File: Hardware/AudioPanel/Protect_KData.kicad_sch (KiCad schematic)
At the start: 34 parts

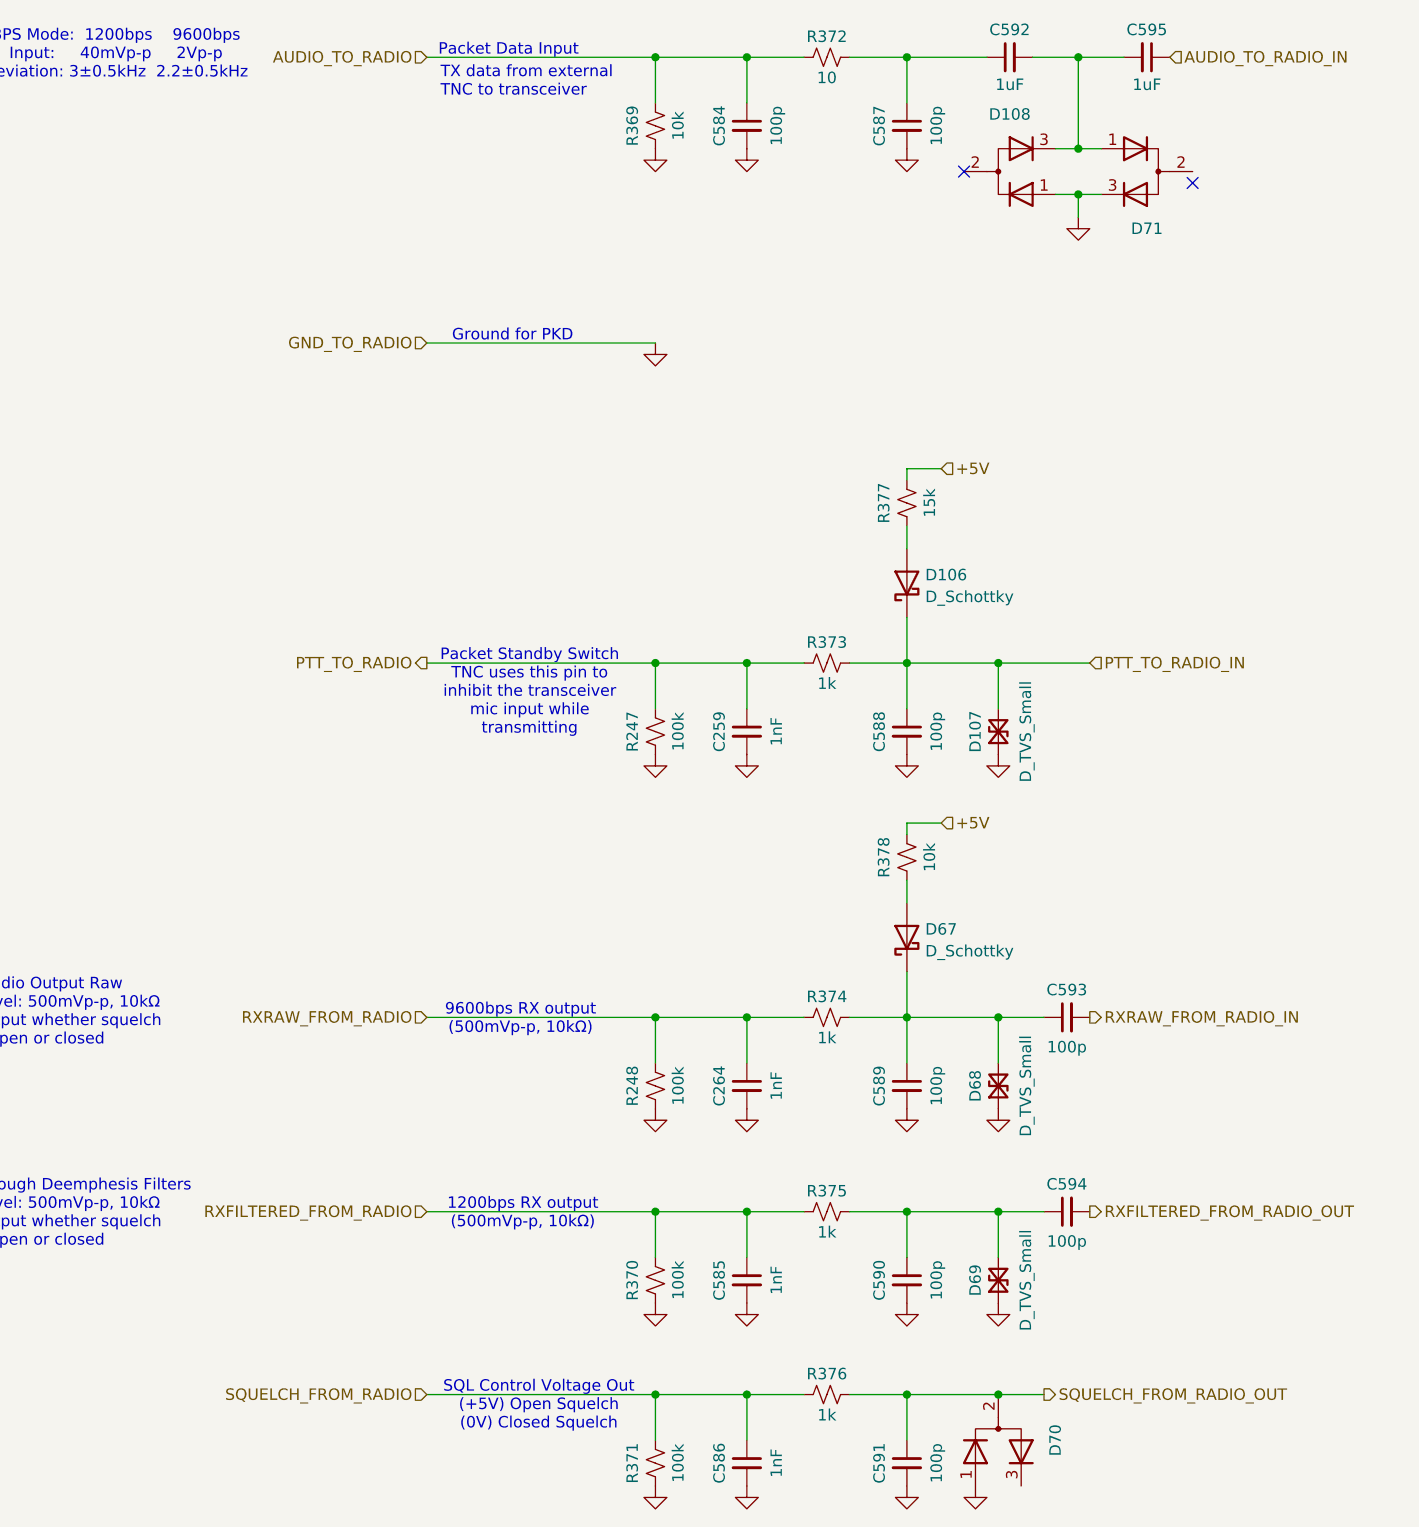
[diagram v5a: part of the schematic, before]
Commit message: Realized that I need to rethink how I'm going to mix the radio audio with the stereo audio
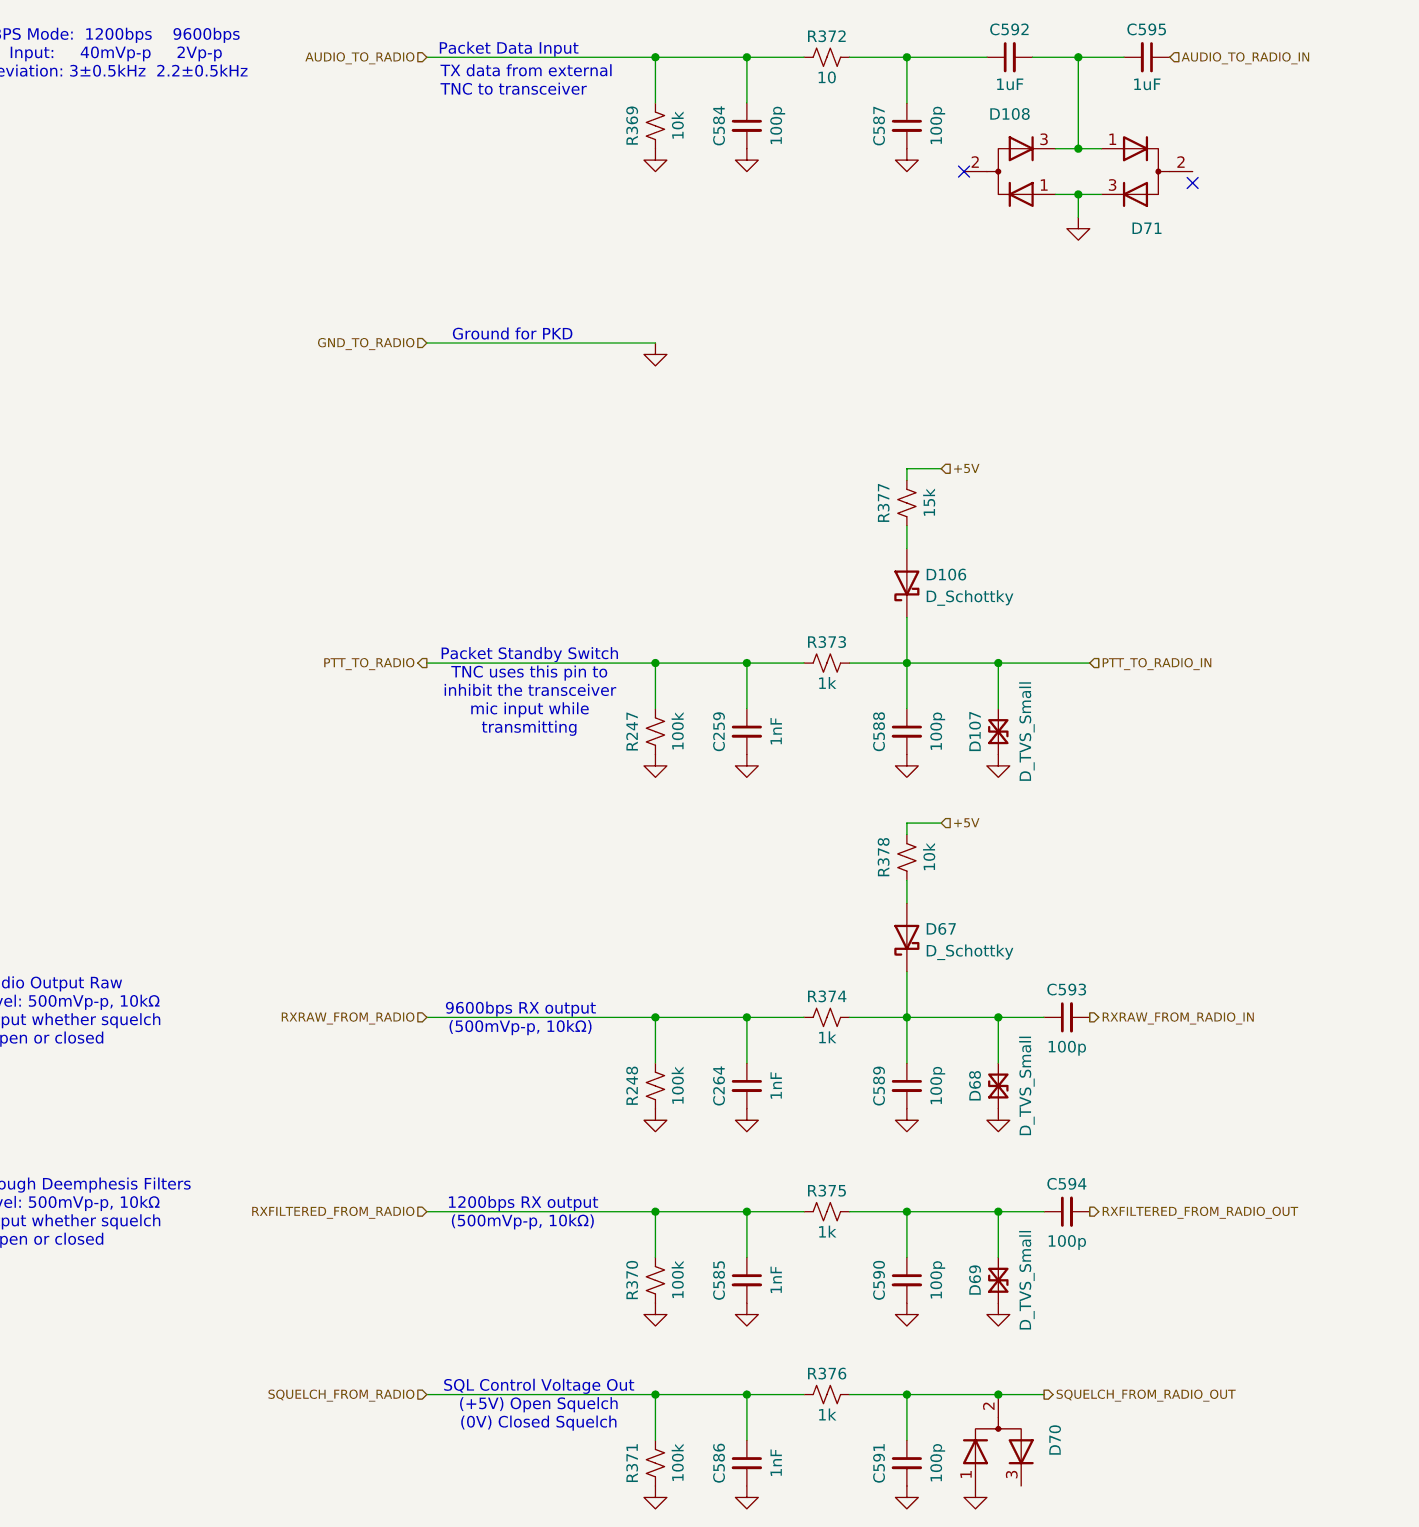
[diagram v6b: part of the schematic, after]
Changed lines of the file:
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@@
 		(effects
 			(font
-				(size 1.27 1.27)
+				(size 1 1)
 			)
 			(justify right)
@@
 		(effects
 			(font
-				(size 1.27 1.27)
+				(size 1 1)
 			)
 			(justify left)
@@
 		(effects
 			(font
-				(size 1.27 1.27)
+				(size 1 1)
 			)
 			(justify right)
@@
 		(effects
 			(font
-				(size 1.27 1.27)
+				(size 1 1)
 			)
 			(justify left)
@@
 		(effects
 			(font
-				(size 1.27 1.27)
+				(size 1 1)
 			)
 			(justify right)
@@
 		(effects
 			(font
-				(size 1.27 1.27)
+				(size 1 1)
 			)
 			(justify left)
@@
 		(effects
 			(font
-				(size 1.27 1.27)
+				(size 1 1)
 			)
 			(justify right)
@@
 		(effects
 			(font
-				(size 1.27 1.27)
+				(size 1 1)
 			)
 			(justify right)
@@
 		(effects
 			(font
-				(size 1.27 1.27)
+				(size 1 1)
 			)
 			(justify left)
@@
 		(effects
 			(font
-				(size 1.27 1.27)
+				(size 1 1)
 			)
 			(justify right)
@@
 		(effects
 			(font
-				(size 1.27 1.27)
+				(size 1 1)
 			)
 			(justify left)
@@
 		(effects
 			(font
-				(size 1.27 1.27)
+				(size 1 1)
 			)
 			(justify left)
@@
 		(effects
 			(font
-				(size 1.27 1.27)
+				(size 1 1)
 			)
 			(justify left)

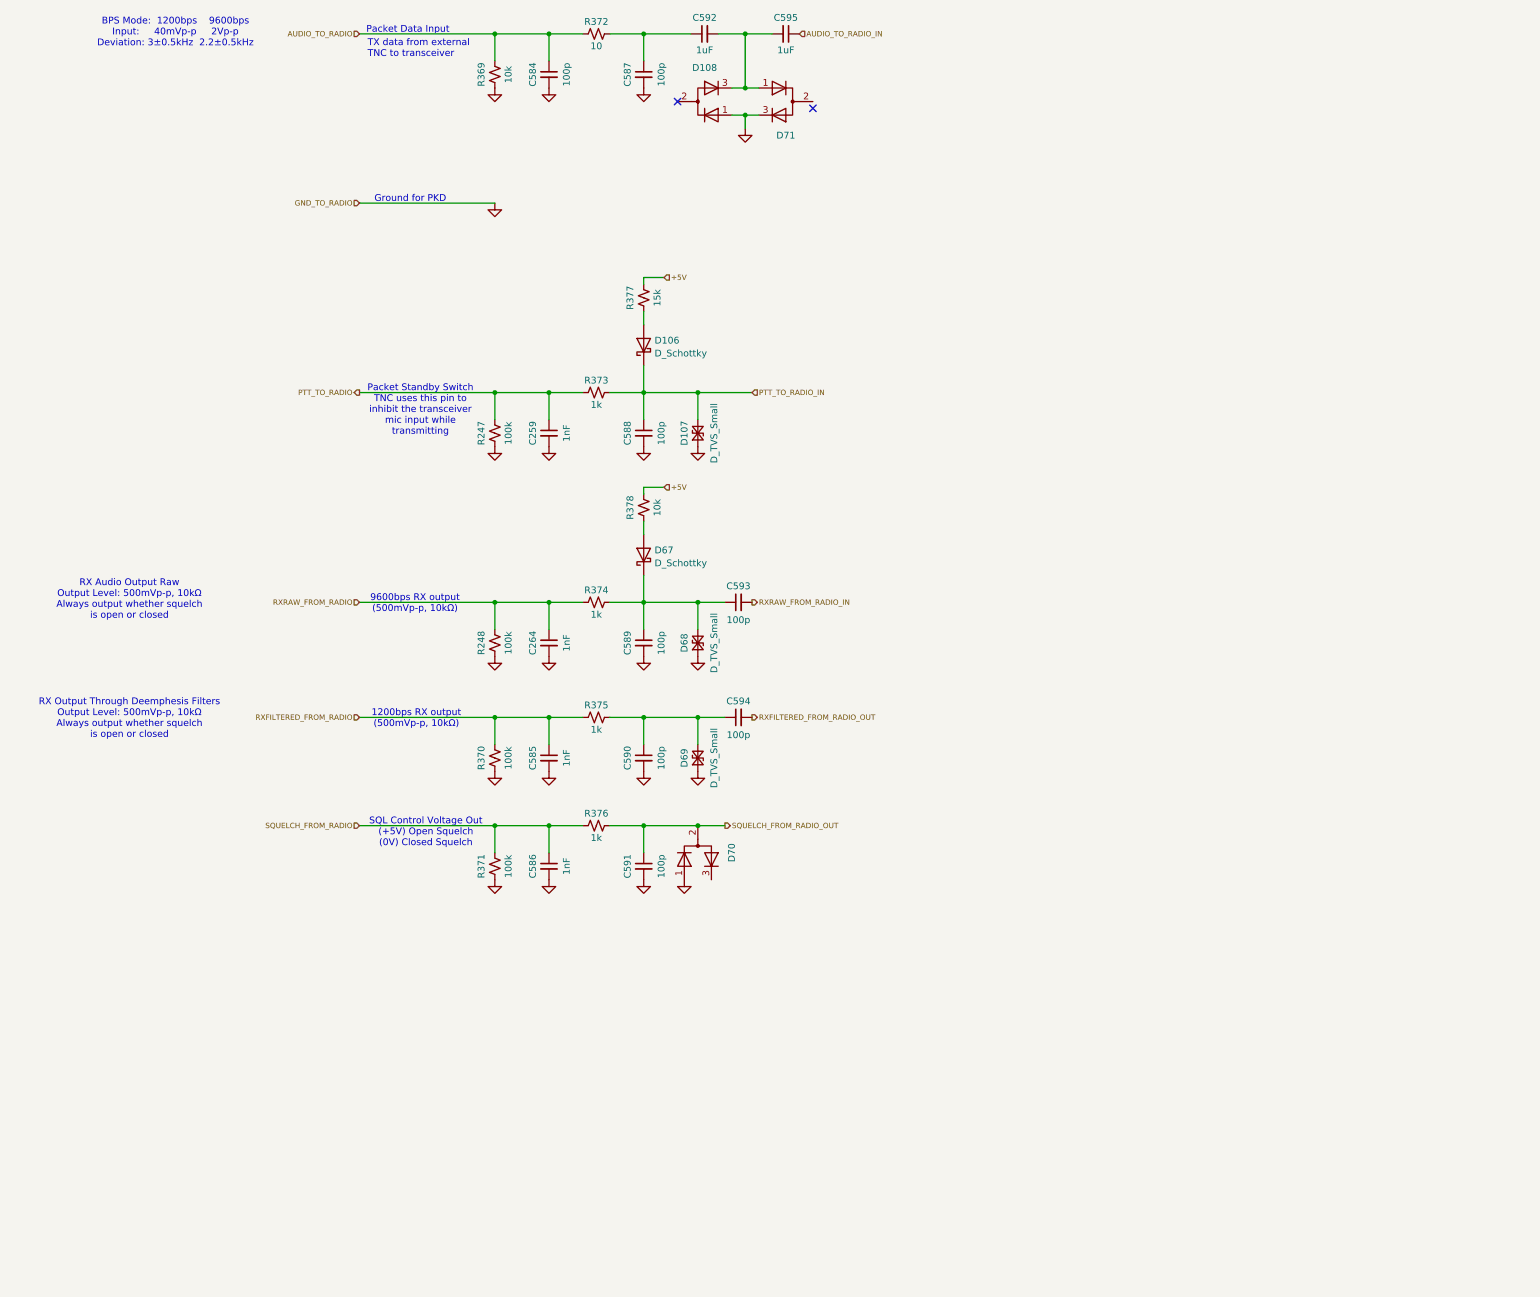
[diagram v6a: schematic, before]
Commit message: Added speaker and headphone audio switching
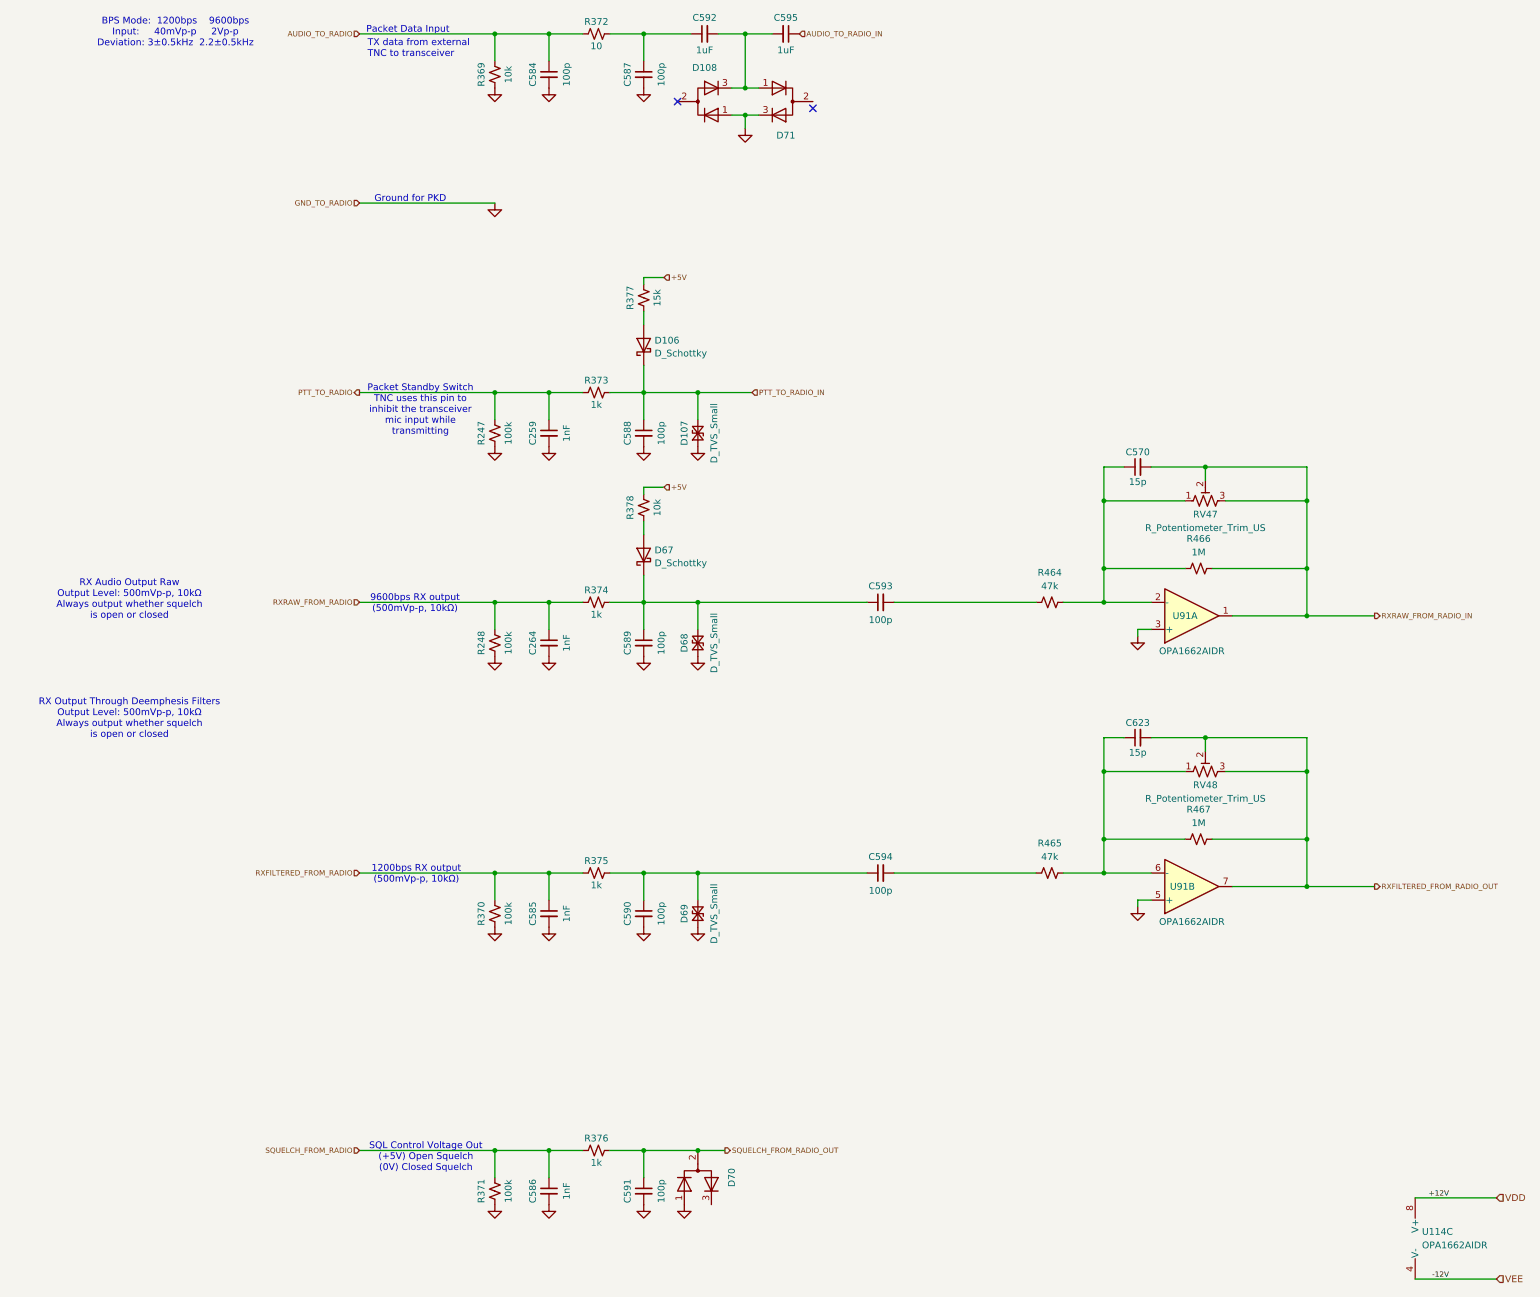
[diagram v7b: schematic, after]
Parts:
- added C570, C623: 15p, symbol Device:C_Small
- added R464, R465: 47k, symbol Device:R_Small_US
- added R466, R467: 1M, symbol Device:R_Small_US
- added RV47, RV48: R_Potentiometer_Trim_US, symbol Device:R_Potentiometer_Trim_US
- added U114, U91: OPA1662AIDR, Package_SO:SOIC-8_3.9x4.9mm_P1.27mm, symbol Amplifier_Operational:OPA1656ID
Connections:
- net GND: now also U91.3 (+), U91.5 (+)
- net RXFILTERED_FROM_RADIO_OUT: now also C623.2, R467.2, RV48.2, RV48.3, U91.7; no longer C594.2
- net RXRAW_FROM_RADIO_IN: now also C570.2, R466.2, RV47.2, RV47.3, U91.1; no longer C593.2
- new net: C594.2, R465.1
- new net: C623.1, R465.2, R467.1, RV48.1, U91.6 (-)
- new net: C570.1, R464.2, R466.1, RV47.1, U91.2 (-)
- new net: C593.2, R464.1
- new net VDD: U114.8 (V+)
- new net VEE: U114.4 (V-)
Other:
- moved on the sheet: C585, C586, C590, C591, C593, C594, D69, D70, R370, R371, R375, R376
